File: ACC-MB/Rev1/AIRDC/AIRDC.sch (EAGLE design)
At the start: 6 parts

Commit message: update
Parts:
- added LED1, LED2: (no value), ACC-MB-R0:LED3MM
- added R2, R4: (no value), ACC-MB-R0:R-US_R0805
- added X13: 5566-4, ACC-MB-R0:5566-4
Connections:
- new net N$1: LED2.C, R2.2
- new net N$5: LED1.C, R4.2
- net AUX_A1: now also U$2.10, U$2.4, U$2.5, U$2.9, X13-1.S, X13-2.S; no longer U$2.1, U$2.2, U$2.6, U$2.7
- net AUX_A2: now also U$2.1, U$2.2, U$2.6, U$2.7, X13-3.S, X13-4.S; no longer U$2.10, U$2.4, U$2.5, U$2.9
- net COIL_X1: now also LED1.A
- net COIL_X2: now also LED2.A
- net GND: now also R2.1, R4.1
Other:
- moved on the sheet: U$2
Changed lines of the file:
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@@
 <part name="FRAME3" library="ACC-MB-R0" deviceset="A3L-LOC" device=""/>
 <part name="U$1" library="ACC-MB-R0" library_urn="urn:adsk.eagle:library:13324935" deviceset="GV224" device="" package3d_urn="urn:adsk.eagle:package:13209922/2"/>
-<part name="U$2" library="ACC-MB-R0" library_urn="urn:adsk.eagle:library:13208985" deviceset="15-24-6100" device=""/>
-<part name="U$3" library="ACC-MB-R0" library_urn="urn:adsk.eagle:library:13208985" deviceset="15-24-6100" device=""/>
-<part name="C1" library="Main" deviceset="AIR_HOLDUP_CAP" device="" value="15000u"/>
-<part name="D1" library="Main" deviceset="AIR_HOLDUP_DIODE" device="" value="10A"/>
-<part name="R1" library="Main" deviceset="AIR_HOLDUP_RESISTOR" device="" value="100"/>
-<part name="GND1" library="Main" deviceset="GND" device=""/>
-<part name="GND2" library="Main" deviceset="GND" device=""/>
+<part name="U$2" library="ACC-MB-R0" library_urn="urn:adsk.eagle:library:13208985" deviceset="15-24-6100" device="" package3d_urn="urn:adsk.eagle:package:14396594/2"/>
+<part name="U$3" library="ACC-MB-R0" library_urn="urn:adsk.eagle:library:13208985" deviceset="15-24-6100" device="" package3d_urn="urn:adsk.eagle:package:14396594/2"/>
+<part name="C1" library="Main" library_urn="urn:adsk.eagle:library:14107900" deviceset="AIR_HOLDUP_CAP" device="" package3d_urn="urn:adsk.eagle:package:14108258/2" value="15000u"/>
+<part name="D1" library="Main" library_urn="urn:adsk.eagle:library:14107900" deviceset="AIR_HOLDUP_DIODE" device="" package3d_urn="urn:adsk.eagle:package:14108257/2" value="10A"/>
+<part name="R1" library="Main" library_urn="urn:adsk.eagle:library:14107900" deviceset="AIR_HOLDUP_RESISTOR" device="" package3d_urn="urn:adsk.eagle:package:14108256/1" value="100"/>
+<part name="GND1" library="Main" library_urn="urn:adsk.eagle:library:14107900" deviceset="GND" device=""/>
+<part name="GND2" library="Main" library_urn="urn:adsk.eagle:library:14107900" deviceset="GND" device=""/>
+<part name="X13" library="ACC-MB-R0" library_urn="urn:adsk.eagle:library:13208985" deviceset="5566-4" device="" package3d_urn="urn:adsk.eagle:package:14396878/2"/>
+<part name="LED1" library="ACC-MB-R0" library_urn="urn:adsk.eagle:library:13208985" deviceset="LED" device="3MM" package3d_urn="urn:adsk.eagle:package:15797/1"/>
+<part name="R4" library="ACC-MB-R0" library_urn="urn:adsk.eagle:library:13208985" deviceset="R-US_" device="R0805" package3d_urn="urn:adsk.eagle:package:13209583/1"/>
+<part name="GND3" library="ACC-MB-R0" library_urn="urn:adsk.eagle:library:13208985" deviceset="GND" device=""/>
+<part name="LED2" library="ACC-MB-R0" library_urn="urn:adsk.eagle:library:13208985" deviceset="LED" device="3MM" package3d_urn="urn:adsk.eagle:package:15797/1"/>
+<part name="R2" library="ACC-MB-R0" library_urn="urn:adsk.eagle:library:13208985" deviceset="R-US_" device="R0805" package3d_urn="urn:adsk.eagle:package:13209583/1"/>
+<part name="GND4" library="ACC-MB-R0" library_urn="urn:adsk.eagle:library:13208985" deviceset="GND" device=""/>
 </parts>
 <sheets>
@@
 </instance>
 <instance part="U$1" gate="G$1" x="116.84" y="132.08"/>
-<instance part="U$2" gate="G$1" x="111.76" y="73.66"/>
+<instance part="U$2" gate="G$1" x="116.84" y="55.88" rot="R180"/>
 <instance part="U$3" gate="G$1" x="172.72" y="73.66"/>
 <instance part="C1" gate="G$1" x="99.06" y="129.54" smashed="yes">
@@
 <instance part="GND1" gate="1" x="99.06" y="114.3"/>
 <instance part="GND2" gate="1" x="175.26" y="55.88"/>
+<instance part="X13" gate="-1" x="127" y="50.8"/>
+<instance part="X13" gate="-2" x="127" y="48.26"/>
+<instance part="X13" gate="-3" x="101.6" y="48.26" rot="R180"/>
+<instance part="X13" gate="-4" x="101.6" y="50.8" rot="R180"/>
+<instance part="LED1" gate="G$1" x="71.12" y="137.16"/>
+<instance part="R4" gate="G$1" x="71.12" y="123.19" rot="R90"/>
+<instance part="GND3" gate="1" x="71.12" y="113.03"/>
+<instance part="LED2" gate="G$1" x="152.4" y="137.16"/>
+<instance part="R2" gate="G$1" x="152.4" y="123.19" rot="R90"/>
+<instance part="GND4" gate="1" x="152.4" y="113.03"/>
 </instances>
 <busses>
@@
 </segment>
 <segment>
-<pinref part="U$2" gate="G$1" pin="9"/>
-<wire x1="111.76" y1="81.28" x2="109.22" y2="81.28" width="0.1524" layer="91"/>
-<pinref part="U$2" gate="G$1" pin="10"/>
-<wire x1="109.22" y1="81.28" x2="104.14" y2="81.28" width="0.1524" layer="91"/>
-<junction x="109.22" y="81.28"/>
-<wire x1="104.14" y1="81.28" x2="104.14" y2="68.58" width="0.1524" layer="91"/>
-<pinref part="U$2" gate="G$1" pin="4"/>
-<wire x1="104.14" y1="68.58" x2="109.22" y2="68.58" width="0.1524" layer="91"/>
-<pinref part="U$2" gate="G$1" pin="5"/>
-<wire x1="109.22" y1="68.58" x2="111.76" y2="68.58" width="0.1524" layer="91"/>
-<junction x="109.22" y="68.58"/>
-<label x="104.14" y="81.28" size="1.778" layer="95"/>
+<wire x1="111.76" y1="60.96" x2="109.22" y2="60.96" width="0.1524" layer="91"/>
+<wire x1="109.22" y1="60.96" x2="104.14" y2="60.96" width="0.1524" layer="91"/>
+<wire x1="104.14" y1="60.96" x2="104.14" y2="50.8" width="0.1524" layer="91"/>
+<wire x1="104.14" y1="50.8" x2="104.14" y2="48.26" width="0.1524" layer="91"/>
+<wire x1="104.14" y1="48.26" x2="109.22" y2="48.26" width="0.1524" layer="91"/>
+<label x="104.14" y="60.96" size="1.778" layer="95"/>
+<pinref part="U$2" gate="G$1" pin="1"/>
+<junction x="109.22" y="60.96"/>
+<pinref part="U$2" gate="G$1" pin="6"/>
+<wire x1="109.22" y1="48.26" x2="111.76" y2="48.26" width="0.1524" layer="91"/>
+<junction x="109.22" y="48.26"/>
+<pinref part="U$2" gate="G$1" pin="2"/>
+<pinref part="U$2" gate="G$1" pin="7"/>
+<pinref part="X13" gate="-3" pin="S"/>
+<junction x="104.14" y="48.26"/>
+<pinref part="X13" gate="-4" pin="S"/>
+<junction x="104.14" y="50.8"/>
 </segment>
 </net>
@@
 <wire x1="142.24" y1="139.7" x2="149.86" y2="139.7" width="0.1524" layer="91"/>
 <label x="162.56" y="139.7" size="1.778" layer="95"/>
-<wire x1="149.86" y1="139.7" x2="172.72" y2="139.7" width="0.1524" layer="91"/>
+<wire x1="149.86" y1="139.7" x2="152.4" y2="139.7" width="0.1524" layer="91"/>
+<pinref part="LED2" gate="G$1" pin="A"/>
+<wire x1="152.4" y1="139.7" x2="172.72" y2="139.7" width="0.1524" layer="91"/>
+<junction x="152.4" y="139.7"/>
 </segment>
 <segment>
@@
 </segment>
 <segment>
-<pinref part="U$2" gate="G$1" pin="7"/>
-<pinref part="U$2" gate="G$1" pin="6"/>
-<wire x1="116.84" y1="81.28" x2="119.38" y2="81.28" width="0.1524" layer="91"/>
-<wire x1="119.38" y1="81.28" x2="124.46" y2="81.28" width="0.1524" layer="91"/>
-<junction x="119.38" y="81.28"/>
-<wire x1="124.46" y1="81.28" x2="124.46" y2="68.58" width="0.1524" layer="91"/>
-<pinref part="U$2" gate="G$1" pin="2"/>
-<wire x1="124.46" y1="68.58" x2="119.38" y2="68.58" width="0.1524" layer="91"/>
-<pinref part="U$2" gate="G$1" pin="1"/>
-<wire x1="119.38" y1="68.58" x2="116.84" y2="68.58" width="0.1524" layer="91"/>
-<junction x="119.38" y="68.58"/>
-<label x="116.84" y="81.28" size="1.778" layer="95"/>
+<wire x1="116.84" y1="60.96" x2="119.38" y2="60.96" width="0.1524" layer="91"/>
+<wire x1="119.38" y1="60.96" x2="124.46" y2="60.96" width="0.1524" layer="91"/>
+<wire x1="124.46" y1="60.96" x2="124.46" y2="50.8" width="0.1524" layer="91"/>
+<wire x1="124.46" y1="50.8" x2="124.46" y2="48.26" width="0.1524" layer="91"/>
+<wire x1="124.46" y1="48.26" x2="119.38" y2="48.26" width="0.1524" layer="91"/>
+<label x="116.84" y="60.96" size="1.778" layer="95"/>
+<pinref part="U$2" gate="G$1" pin="4"/>
+<pinref part="U$2" gate="G$1" pin="5"/>
+<junction x="119.38" y="60.96"/>
+<pinref part="U$2" gate="G$1" pin="9"/>
+<pinref part="U$2" gate="G$1" pin="10"/>
+<wire x1="119.38" y1="48.26" x2="116.84" y2="48.26" width="0.1524" layer="91"/>
+<junction x="119.38" y="48.26"/>
+<pinref part="X13" gate="-1" pin="S"/>
+<junction x="124.46" y="50.8"/>
+<pinref part="X13" gate="-2" pin="S"/>
+<junction x="124.46" y="48.26"/>
 </segment>
 </net>
@@
 <label x="55.88" y="139.7" size="1.778" layer="95"/>
 <wire x1="106.68" y1="139.7" x2="81.28" y2="139.7" width="0.1524" layer="91"/>
-<wire x1="81.28" y1="139.7" x2="55.88" y2="139.7" width="0.1524" layer="91"/>
+<wire x1="81.28" y1="139.7" x2="71.12" y2="139.7" width="0.1524" layer="91"/>
 <pinref part="R1" gate="G$1" pin="1"/>
+<wire x1="71.12" y1="139.7" x2="55.88" y2="139.7" width="0.1524" layer="91"/>
 <wire x1="83.82" y1="132.08" x2="81.28" y2="132.08" width="0.1524" layer="91"/>
 <wire x1="81.28" y1="132.08" x2="81.28" y2="139.7" width="0.1524" layer="91"/>
@@
 <wire x1="106.68" y1="137.16" x2="106.68" y2="139.7" width="0.1524" layer="91"/>
 <junction x="106.68" y="139.7"/>
+<pinref part="LED1" gate="G$1" pin="A"/>
+<junction x="71.12" y="139.7"/>
 </segment>
 <segment>
@@
 <wire x1="175.26" y1="91.44" x2="175.26" y2="81.28" width="0.1524" layer="91"/>
 </segment>
-</net>
+<segment>
+<pinref part="GND3" gate="1" pin="GND"/>
+<pinref part="R4" gate="G$1" pin="1"/>
+<wire x1="71.12" y1="115.57" x2="71.12" y2="118.11" width="0.1524" layer="91"/>
+</segment>
+<segment>
+<pinref part="GND4" gate="1" pin="GND"/>
+<pinref part="R2" gate="G$1" pin="1"/>
+<wire x1="152.4" y1="115.57" x2="152.4" y2="118.11" width="0.1524" layer="91"/>
+</segment>
+</net>
+<net name="N$5" class="0">
+<segment>
+<pinref part="R4" gate="G$1" pin="2"/>
+<pinref part="LED1" gate="G$1" pin="C"/>
+<wire x1="71.12" y1="128.27" x2="71.12" y2="132.08" width="0.1524" layer="91"/>
+</segment>
+</net>
+<net name="N$1" class="0">
+<segment>
+<pinref part="R2" gate="G$1" pin="2"/>
+<pinref part="LED2" gate="G$1" pin="C"/>
+<wire x1="152.4" y1="128.27" x2="152.4" y2="132.08" width="0.1524" layer="91"/>
+</segment>
+</net>

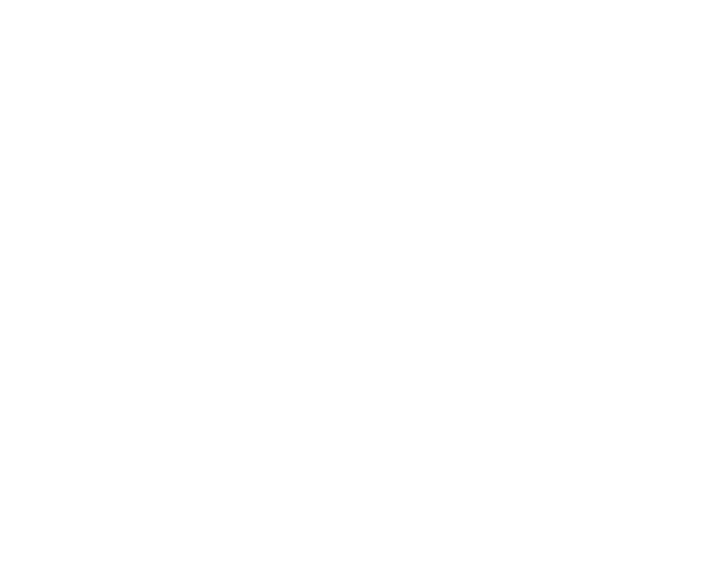
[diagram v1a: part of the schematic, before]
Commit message: 7792 added to all DC
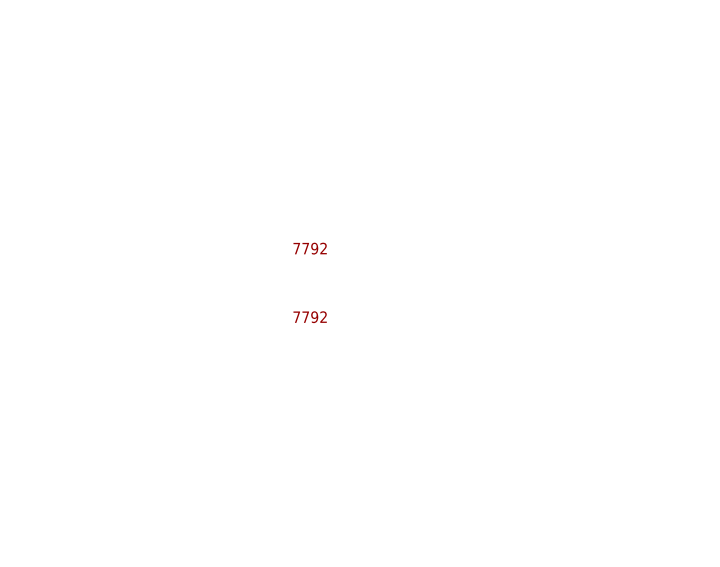
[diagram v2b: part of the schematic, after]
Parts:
- added U$4, U$5: 7792, ACC-MB-R0:7792
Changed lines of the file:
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@@
 <part name="R2" library="ACC-MB-R0" library_urn="urn:adsk.eagle:library:13208985" deviceset="R-US_" device="R0805" package3d_urn="urn:adsk.eagle:package:13209583/1"/>
 <part name="GND4" library="ACC-MB-R0" library_urn="urn:adsk.eagle:library:13208985" deviceset="GND" device=""/>
+<part name="U$4" library="ACC-MB-R0" library_urn="urn:adsk.eagle:library:13208985" deviceset="7792" device="" package3d_urn="urn:adsk.eagle:package:14511284/2"/>
+<part name="U$5" library="ACC-MB-R0" library_urn="urn:adsk.eagle:library:13208985" deviceset="7792" device="" package3d_urn="urn:adsk.eagle:package:14511284/2"/>
 </parts>
 <sheets>
@@
 <instance part="R2" gate="G$1" x="152.4" y="123.19" rot="R90"/>
 <instance part="GND4" gate="1" x="152.4" y="113.03"/>
+<instance part="U$4" gate="G$1" x="35.56" y="200.66"/>
+<instance part="U$5" gate="G$1" x="35.56" y="193.04"/>
 </instances>
 <busses>
